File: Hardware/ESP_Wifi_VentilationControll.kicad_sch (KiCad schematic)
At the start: 35 parts, among them J1 programming, Q1 2N3904, Q2 2N3904, SW1 RST, SW2 BOOT, U1 LM1117-3.3, U2 ESP-12E, U3 ILD207T_D207, U4 ILD207T_D207, U5 XD-45_MH_MINI

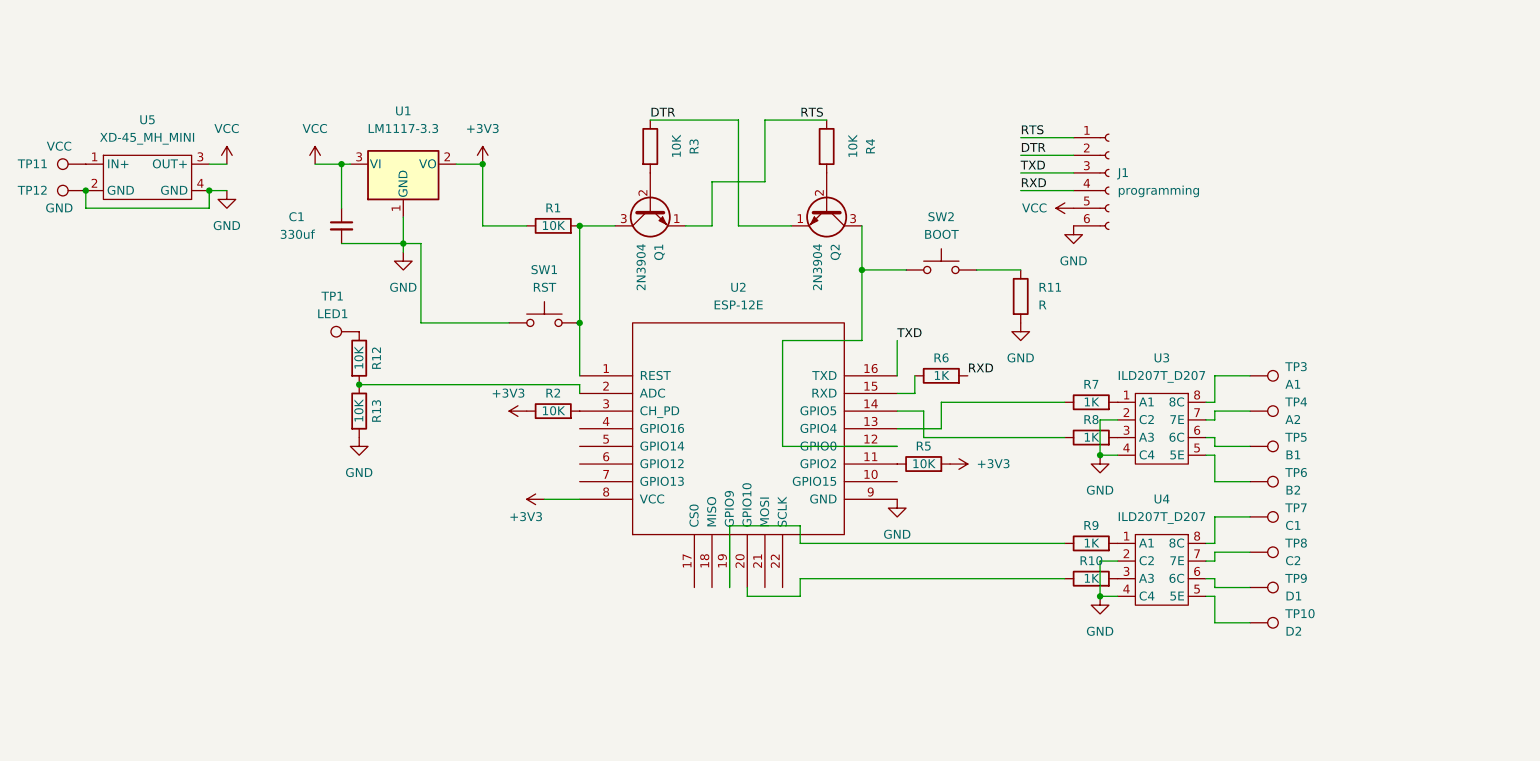
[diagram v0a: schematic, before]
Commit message: added smoothing capacitors
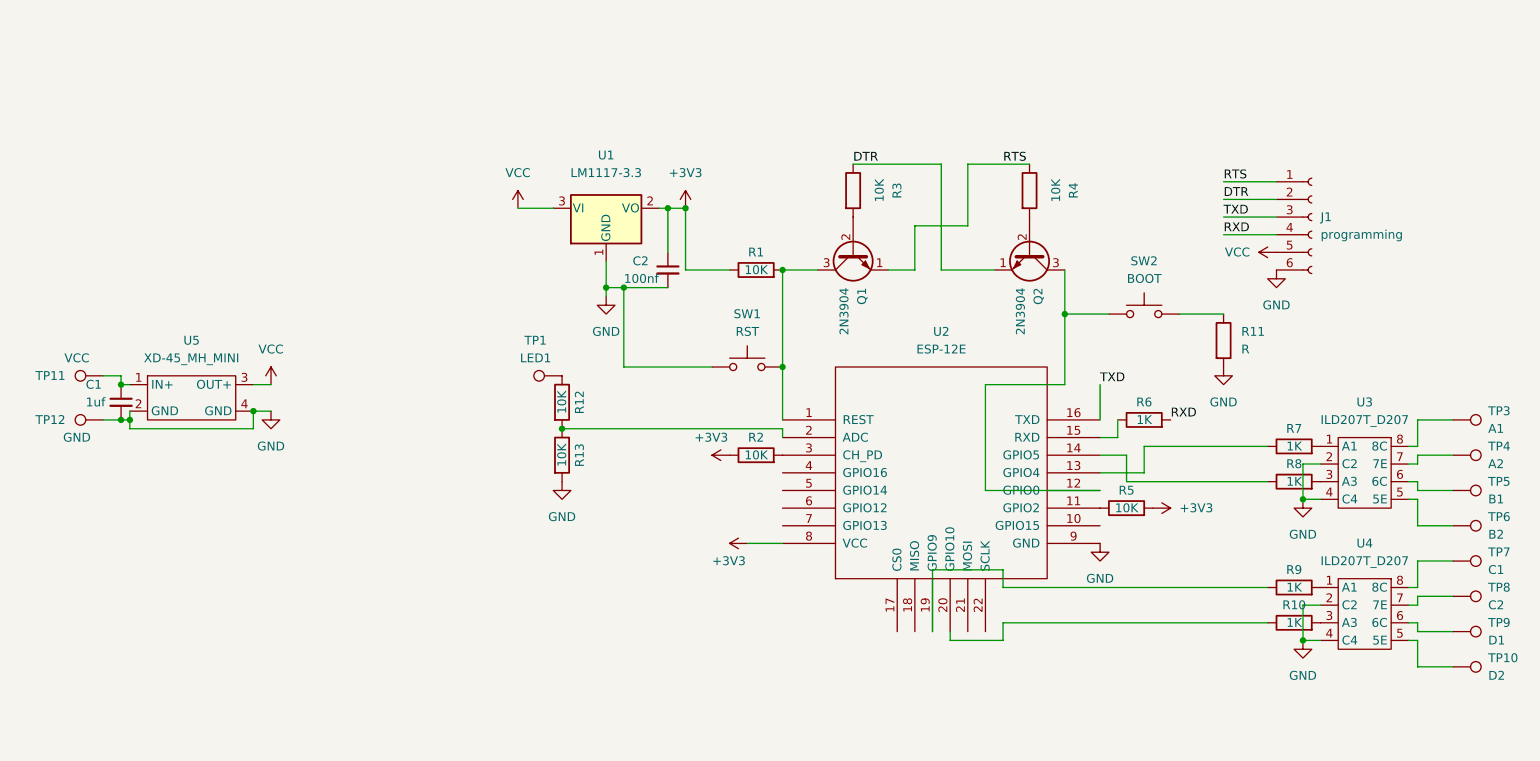
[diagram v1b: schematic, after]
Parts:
- added C2: 100nf, Capacitor_SMD:C_0805_2012Metric, symbol Device:C_Small
- C1: value 330uf -> 1uf; footprint Capacitor_THT:CP_Radial_D8.0mm_P3.50mm -> Capacitor_SMD:C_0805_2012Metric
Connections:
- net +3V3: now also C2.1
- net GND: now also C2.2
- net VCC: no longer C1.1
- net at TP11.1, U5.1 (IN+): now also C1.1
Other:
- moved on the sheet: C1, J1, Q1, Q2, R1, R10, R11, R12, R13, R2, R3, R4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

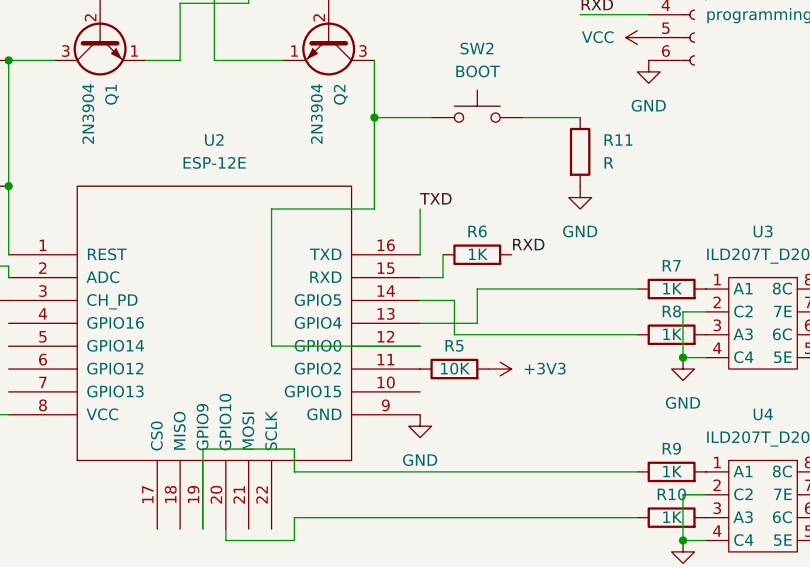
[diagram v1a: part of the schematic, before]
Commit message: added status LED
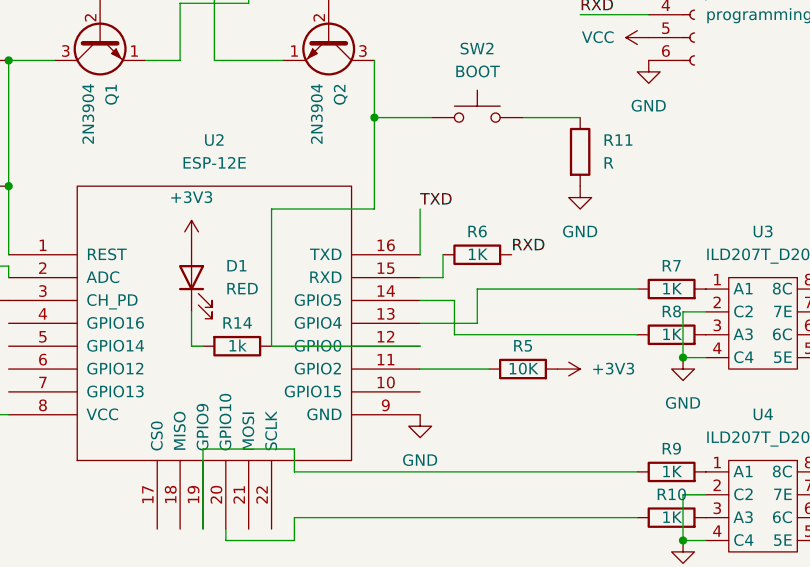
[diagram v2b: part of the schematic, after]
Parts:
- added D1: RED, LED_SMD:LED_1206_3216Metric, symbol Device:LED
- added R14: 1k, Resistor_SMD:R_1206_3216Metric, symbol Device:R
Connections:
- net +3V3: now also D1.2 (A)
- net at Q2.3 (C), SW2.1, U2.12 (GPIO0): now also R14.1
- new net: D1.1 (K), R14.2
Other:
- moved on the sheet: R5
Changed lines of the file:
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@@
+    (stroke (width 0) (type default) (color 0 0 0 0))
+  )
+  (wire (pts (xy 170.18 114.3) (xy 171.45 114.3))
     (stroke (width 0) (type default) (color 0 0 0 0))
   )
@@
     (stroke (width 0) (type default) (color 0 0 0 0))
   )
+  (wire (pts (xy 170.18 110.49) (xy 170.18 114.3))
+    (stroke (width 0) (type default) (color 0 0 0 0))
+  )
   (wire (pts (xy 181.61 133.35) (xy 181.61 135.89))
     (stroke (width 0) (type default) (color 0 0 0 0))
@@
   )
   (wire (pts (xy 54.61 104.14) (xy 55.88 104.14))
+    (stroke (width 0) (type default) (color 0 0 0 0))
+  )
+  (wire (pts (xy 203.2 116.84) (xy 195.58 116.84))
     (stroke (width 0) (type default) (color 0 0 0 0))
   )
@@
     (pin "1")
   )
-  (symbol (lib_id "Device:R") (at 199.39 116.84 90) (unit 1)
-    (in_bom yes) (on_board yes)
-    (property "Reference" "R5" (id 0) (at 199.39 114.3 90))
-    (property "Value" "10K" (id 1) (at 199.39 116.84 90))
-    (property "Footprint" "Resistor_SMD:R_1206_3216Metric" (id 2) (at 199.39 118.618 90)
-      (effects (font (size 1.27 1.27)) hide)
-    )
-    (property "Datasheet" "~" (id 3) (at 199.39 116.84 0)
+  (symbol (lib_id "Device:R") (at 207.01 116.84 90) (unit 1)
+    (in_bom yes) (on_board yes)
+    (property "Reference" "R5" (id 0) (at 207.01 114.3 90))
+    (property "Value" "10K" (id 1) (at 207.01 116.84 90))
+    (property "Footprint" "Resistor_SMD:R_1206_3216Metric" (id 2) (at 207.01 118.618 90)
+      (effects (font (size 1.27 1.27)) hide)
+    )
+    (property "Datasheet" "~" (id 3) (at 207.01 116.84 0)
       (effects (font (size 1.27 1.27)) hide)
     )
@@
     )
     (pin "1")
+  )
+  (symbol (lib_id "Device:R") (at 175.26 114.3 270) (unit 1)
+    (in_bom yes) (on_board yes)
+    (property "Reference" "R14" (id 0) (at 175.26 111.76 90))
+    (property "Value" "1k" (id 1) (at 175.26 114.3 90))
+    (property "Footprint" "Resistor_SMD:R_1206_3216Metric" (id 2) (at 175.26 112.522 90)
+      (effects (font (size 1.27 1.27)) hide)
+    )
+    (property "Datasheet" "~" (id 3) (at 175.26 114.3 0)
+      (effects (font (size 1.27 1.27)) hide)
+    )
+    (pin "1")
+    (pin "2")
   )
   (symbol (lib_id "Connector:TestPoint") (at 246.38 134.62 270) (unit 1)
@@
     (pin "2")
   )
-  (symbol (lib_id "power:+3V3") (at 203.2 116.84 270) (unit 1)
-    (in_bom yes) (on_board yes) (fields_autoplaced)
-    (property "Reference" "#PWR07" (id 0) (at 199.39 116.84 0)
-      (effects (font (size 1.27 1.27)) hide)
-    )
-    (property "Value" "+3V3" (id 1) (at 207.01 116.8399 90)
-      (effects (font (size 1.27 1.27)) (justify left))
-    )
-    (property "Footprint" "" (id 2) (at 203.2 116.84 0)
-      (effects (font (size 1.27 1.27)) hide)
-    )
-    (property "Datasheet" "" (id 3) (at 203.2 116.84 0)
+  (symbol (lib_id "power:+3V3") (at 210.82 116.84 270) (unit 1)
+    (in_bom yes) (on_board yes)
+    (property "Reference" "#PWR07" (id 0) (at 207.01 116.84 0)
+      (effects (font (size 1.27 1.27)) hide)
+    )
+    (property "Value" "+3V3" (id 1) (at 214.63 116.84 90)
+      (effects (font (size 1.27 1.27)) (justify left))
+    )
+    (property "Footprint" "" (id 2) (at 210.82 116.84 0)
+      (effects (font (size 1.27 1.27)) hide)
+    )
+    (property "Datasheet" "" (id 3) (at 210.82 116.84 0)
       (effects (font (size 1.27 1.27)) hide)
     )
@@
     (pin "7")
     (pin "8")
+  )
+  (symbol (lib_id "Device:LED") (at 170.18 106.68 90) (unit 1)
+    (in_bom yes) (on_board yes)
+    (property "Reference" "D1" (id 0) (at 173.99 105.41 90)
+      (effects (font (size 1.27 1.27)) (justify right))
+    )
+    (property "Value" "RED" (id 1) (at 173.99 107.95 90)
+      (effects (font (size 1.27 1.27)) (justify right))
+    )
+    (property "Footprint" "LED_SMD:LED_1206_3216Metric" (id 2) (at 170.18 106.68 0)
+      (effects (font (size 1.27 1.27)) hide)
+    )
+    (property "Datasheet" "~" (id 3) (at 170.18 106.68 0)
+      (effects (font (size 1.27 1.27)) hide)
+    )
+    (pin "1")
+    (pin "2")
+  )
+  (symbol (lib_id "power:+3V3") (at 170.18 102.87 0) (unit 1)
+    (in_bom yes) (on_board yes) (fields_autoplaced)
+    (property "Reference" "#PWR0105" (id 0) (at 170.18 106.68 0)
+      (effects (font (size 1.27 1.27)) hide)
+    )
+    (property "Value" "+3V3" (id 1) (at 170.18 97.79 0))
+    (property "Footprint" "" (id 2) (at 170.18 102.87 0)
+      (effects (font (size 1.27 1.27)) hide)
+    )
+    (property "Datasheet" "" (id 3) (at 170.18 102.87 0)
+      (effects (font (size 1.27 1.27)) hide)
+    )
+    (pin "1")
   )
   (symbol (lib_id "Device:R") (at 185.42 71.12 0) (unit 1)
@@
       (reference "#PWR0104") (unit 1) (value "VCC") (footprint "")
     )
+    (path "/b67189bd-47d0-45c6-9b94-c8db2bb97af8"
+      (reference "#PWR0105") (unit 1) (value "+3V3") (footprint "")
+    )
     (path "/b97f56a2-7047-42bc-afed-5139d66aca30"
       (reference "C1") (unit 1) (value "1uf") (footprint "Capacitor_SMD:C_0805_2012Metric")
@@
       (reference "C2") (unit 1) (value "100nf") (footprint "Capacitor_SMD:C_0805_2012Metric")
     )
+    (path "/b0fa91c3-0331-4596-9370-e933e0cffece"
+      (reference "D1") (unit 1) (value "RED") (footprint "LED_SMD:LED_1206_3216Metric")
+    )
     (path "/c08a322f-2c04-40e2-8dca-ef3008ca0260"
       (reference "J1") (unit 1) (value "programming") (footprint "Connector_PinHeader_2.54mm:PinHeader_1x06_P2.54mm_Vertical")
@@
       (reference "R13") (unit 1) (value "10K") (footprint "Resistor_SMD:R_1206_3216Metric")
     )
+    (path "/6dee8330-111b-4001-8f00-ffcb37b85e75"
+      (reference "R14") (unit 1) (value "1k") (footprint "Resistor_SMD:R_1206_3216Metric")
+    )
     (path "/8fbb98cd-d7ce-4148-8987-cf22f55e0e15"

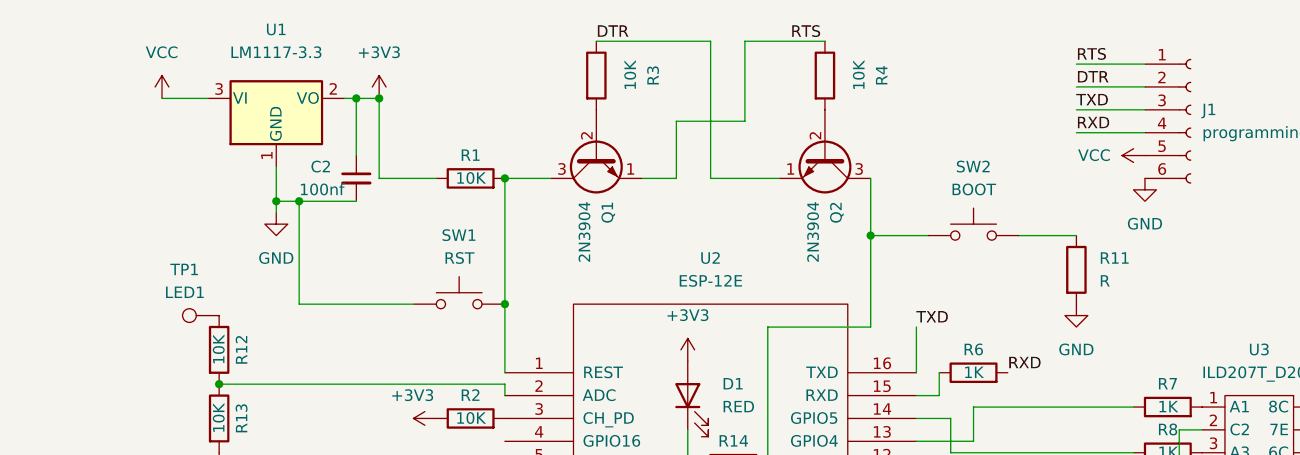
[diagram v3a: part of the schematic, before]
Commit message: added missing resistor values
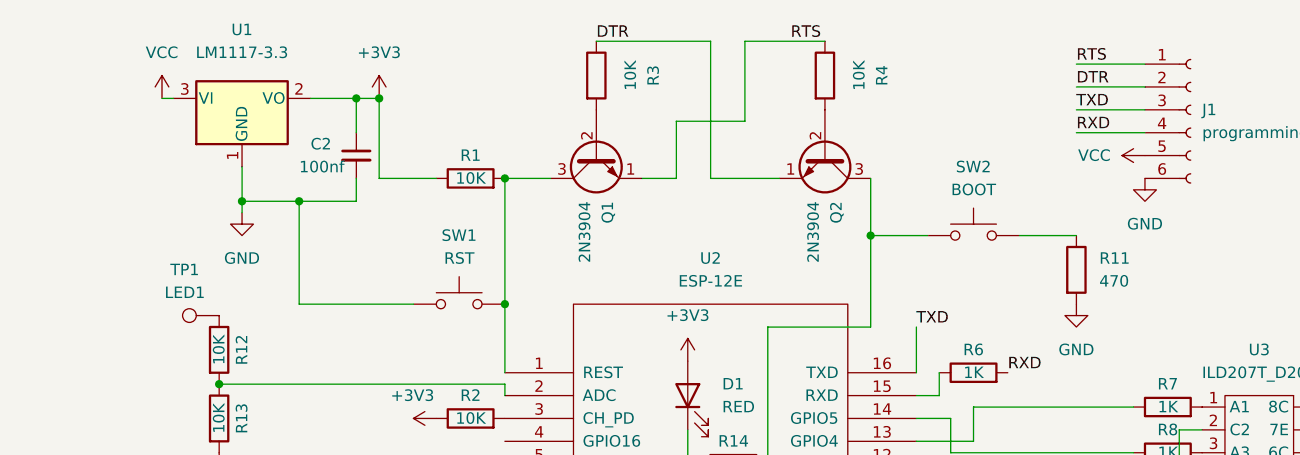
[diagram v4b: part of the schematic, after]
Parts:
- R11: value R -> 470
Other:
- moved on the sheet: C2, U1
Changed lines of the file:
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@@
   (junction (at 224.79 135.89) (diameter 0) (color 0 0 0 0)
   )
+  (junction (at 120.65 85.09) (diameter 0) (color 0 0 0 0)
+  )
   (junction (at 149.86 82.55) (diameter 0) (color 0 0 0 0)
   )
@@
   (junction (at 149.86 96.52) (diameter 0) (color 0 0 0 0)
   )
-  (junction (at 124.46 85.09) (diameter 0) (color 0 0 0 0)
-  )
   (junction (at 54.61 104.14) (diameter 0) (color 0 0 0 0)
   )
@@
     (stroke (width 0) (type default) (color 0 0 0 0))
   )
-  (wire (pts (xy 111.76 73.66) (xy 116.84 73.66))
+  (wire (pts (xy 111.76 73.66) (xy 113.03 73.66))
     (stroke (width 0) (type default) (color 0 0 0 0))
   )
@@
     (stroke (width 0) (type default) (color 0 0 0 0))
   )
-  (wire (pts (xy 124.46 85.09) (xy 124.46 86.36))
-    (stroke (width 0) (type default) (color 0 0 0 0))
-  )
   (wire (pts (xy 171.45 125.73) (xy 171.45 134.62))
     (stroke (width 0) (type default) (color 0 0 0 0))
@@
     (stroke (width 0) (type default) (color 0 0 0 0))
   )
-  (wire (pts (xy 124.46 81.28) (xy 124.46 85.09))
-    (stroke (width 0) (type default) (color 0 0 0 0))
-  )
   (wire (pts (xy 55.88 104.14) (xy 55.88 105.41))
     (stroke (width 0) (type default) (color 0 0 0 0))
   )
-  (wire (pts (xy 124.46 85.09) (xy 127 85.09))
+  (wire (pts (xy 120.65 85.09) (xy 127 85.09))
+    (stroke (width 0) (type default) (color 0 0 0 0))
+  )
+  (wire (pts (xy 120.65 85.09) (xy 120.65 86.36))
     (stroke (width 0) (type default) (color 0 0 0 0))
   )
@@
     (stroke (width 0) (type default) (color 0 0 0 0))
   )
+  (wire (pts (xy 120.65 81.28) (xy 120.65 85.09))
+    (stroke (width 0) (type default) (color 0 0 0 0))
+  )
   (wire (pts (xy 224.79 110.49) (xy 224.79 115.57))
     (stroke (width 0) (type default) (color 0 0 0 0))
@@
     (stroke (width 0) (type default) (color 0 0 0 0))
   )
+  (wire (pts (xy 133.35 82.55) (xy 133.35 85.09))
+    (stroke (width 0) (type default) (color 0 0 0 0))
+  )
   (wire (pts (xy 133.35 73.66) (xy 135.89 73.66))
     (stroke (width 0) (type default) (color 0 0 0 0))
@@
     (stroke (width 0) (type default) (color 0 0 0 0))
   )
+  (wire (pts (xy 133.35 85.09) (xy 127 85.09))
+    (stroke (width 0) (type default) (color 0 0 0 0))
+  )
   (wire (pts (xy 241.3 134.62) (xy 241.3 133.35))
     (stroke (width 0) (type default) (color 0 0 0 0))
@@
     (stroke (width 0) (type default) (color 0 0 0 0))
   )
-  (wire (pts (xy 127 85.09) (xy 133.35 85.09))
-    (stroke (width 0) (type default) (color 0 0 0 0))
-  )
   (wire (pts (xy 199.39 109.22) (xy 199.39 113.03))
     (stroke (width 0) (type default) (color 0 0 0 0))
@@
     (stroke (width 0) (type default) (color 0 0 0 0))
   )
-  (wire (pts (xy 132.08 73.66) (xy 133.35 73.66))
+  (wire (pts (xy 128.27 73.66) (xy 133.35 73.66))
     (stroke (width 0) (type default) (color 0 0 0 0))
   )
@@
     (stroke (width 0) (type default) (color 0 0 0 0))
   )
-  (wire (pts (xy 133.35 73.66) (xy 133.35 80.01))
+  (wire (pts (xy 133.35 73.66) (xy 133.35 77.47))
     (stroke (width 0) (type default) (color 0 0 0 0))
   )
@@
     (pin "1")
   )
-  (symbol (lib_id "power:GND") (at 124.46 86.36 0) (unit 1)
-    (in_bom yes) (on_board yes) (fields_autoplaced)
-    (property "Reference" "#PWR02" (id 0) (at 124.46 92.71 0)
-      (effects (font (size 1.27 1.27)) hide)
-    )
-    (property "Value" "GND" (id 1) (at 124.46 91.44 0))
-    (property "Footprint" "" (id 2) (at 124.46 86.36 0)
-      (effects (font (size 1.27 1.27)) hide)
-    )
-    (property "Datasheet" "" (id 3) (at 124.46 86.36 0)
+  (symbol (lib_id "power:GND") (at 120.65 86.36 0) (unit 1)
+    (in_bom yes) (on_board yes) (fields_autoplaced)
+    (property "Reference" "#PWR02" (id 0) (at 120.65 92.71 0)
+      (effects (font (size 1.27 1.27)) hide)
+    )
+    (property "Value" "GND" (id 1) (at 120.65 91.44 0))
+    (property "Footprint" "" (id 2) (at 120.65 86.36 0)
+      (effects (font (size 1.27 1.27)) hide)
+    )
+    (property "Datasheet" "" (id 3) (at 120.65 86.36 0)
       (effects (font (size 1.27 1.27)) hide)
     )
@@
       (effects (font (size 1.27 1.27)) (justify left))
     )
-    (property "Value" "R" (id 1) (at 215.9 93.9799 0)
+    (property "Value" "470" (id 1) (at 215.9 93.9799 0)
       (effects (font (size 1.27 1.27)) (justify left))
     )
@@
     (pin "1")
   )
-  (symbol (lib_id "Regulator_Linear:LM1117-3.3") (at 124.46 73.66 0) (unit 1)
-    (in_bom yes) (on_board yes) (fields_autoplaced)
-    (property "Reference" "U1" (id 0) (at 124.46 66.04 0))
-    (property "Value" "LM1117-3.3" (id 1) (at 124.46 68.58 0))
-    (property "Footprint" "Package_TO_SOT_SMD:SOT-223-3_TabPin2" (id 2) (at 124.46 73.66 0)
-      (effects (font (size 1.27 1.27)) hide)
-    )
-    (property "Datasheet" "http://www.ti.com/lit/ds/symlink/lm1117.pdf" (id 3) (at 124.46 73.66 0)
+  (symbol (lib_id "Regulator_Linear:LM1117-3.3") (at 120.65 73.66 0) (unit 1)
+    (in_bom yes) (on_board yes) (fields_autoplaced)
+    (property "Reference" "U1" (id 0) (at 120.65 66.04 0))
+    (property "Value" "LM1117-3.3" (id 1) (at 120.65 68.58 0))
+    (property "Footprint" "Package_TO_SOT_SMD:SOT-223-3_TabPin2" (id 2) (at 120.65 73.66 0)
+      (effects (font (size 1.27 1.27)) hide)
+    )
+    (property "Datasheet" "http://www.ti.com/lit/ds/symlink/lm1117.pdf" (id 3) (at 120.65 73.66 0)
       (effects (font (size 1.27 1.27)) hide)
     )
@@
     (pin "1")
   )
-  (symbol (lib_id "Device:C_Small") (at 133.35 82.55 0) (unit 1)
-    (in_bom yes) (on_board yes)
-    (property "Reference" "C2" (id 0) (at 128.27 81.28 0)
-      (effects (font (size 1.27 1.27)) (justify left))
-    )
-    (property "Value" "100nf" (id 1) (at 127 83.82 0)
-      (effects (font (size 1.27 1.27)) (justify left))
-    )
-    (property "Footprint" "Capacitor_SMD:C_0805_2012Metric" (id 2) (at 133.35 82.55 0)
-      (effects (font (size 1.27 1.27)) hide)
-    )
-    (property "Datasheet" "~" (id 3) (at 133.35 82.55 0)
+  (symbol (lib_id "Device:C_Small") (at 133.35 80.01 0) (unit 1)
+    (in_bom yes) (on_board yes)
+    (property "Reference" "C2" (id 0) (at 128.27 78.74 0)
+      (effects (font (size 1.27 1.27)) (justify left))
+    )
+    (property "Value" "100nf" (id 1) (at 127 81.28 0)
+      (effects (font (size 1.27 1.27)) (justify left))
+    )
+    (property "Footprint" "Capacitor_SMD:C_0805_2012Metric" (id 2) (at 133.35 80.01 0)
+      (effects (font (size 1.27 1.27)) hide)
+    )
+    (property "Datasheet" "~" (id 3) (at 133.35 80.01 0)
       (effects (font (size 1.27 1.27)) hide)
     )
@@
     )
     (path "/282a7afe-4662-4116-a040-30c34658a6e1"
-      (reference "R11") (unit 1) (value "R") (footprint "Resistor_SMD:R_1206_3216Metric")
+      (reference "R11") (unit 1) (value "470") (footprint "Resistor_SMD:R_1206_3216Metric")
     )
     (path "/13b0ed11-1428-4d61-9c6e-3adb894373aa"
